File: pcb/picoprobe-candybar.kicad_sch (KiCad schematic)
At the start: 25 parts, among them J1 Conn_IDC_Cable, J2 SWD-UART_PicoprobeCandybar, Q1 BSS806N, SW1 SW-R1-1A-E-1-0, SW2 SLW-156646-5A-N-D, U1 74AUP1T17, U2 74AUP1T17

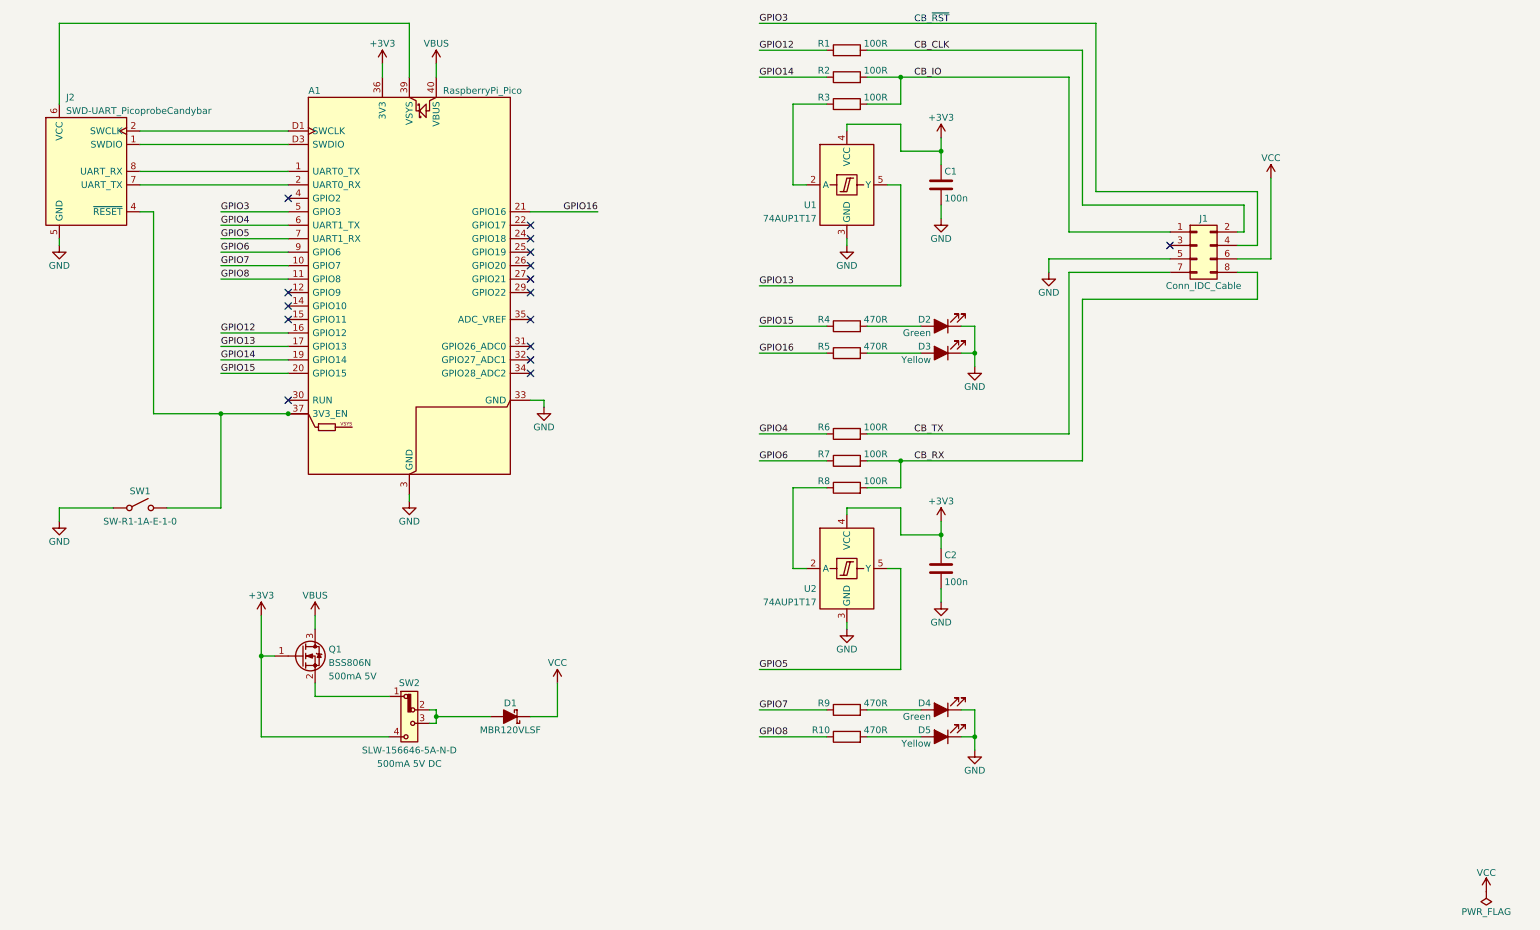
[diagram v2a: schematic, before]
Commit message: Label schematic sections
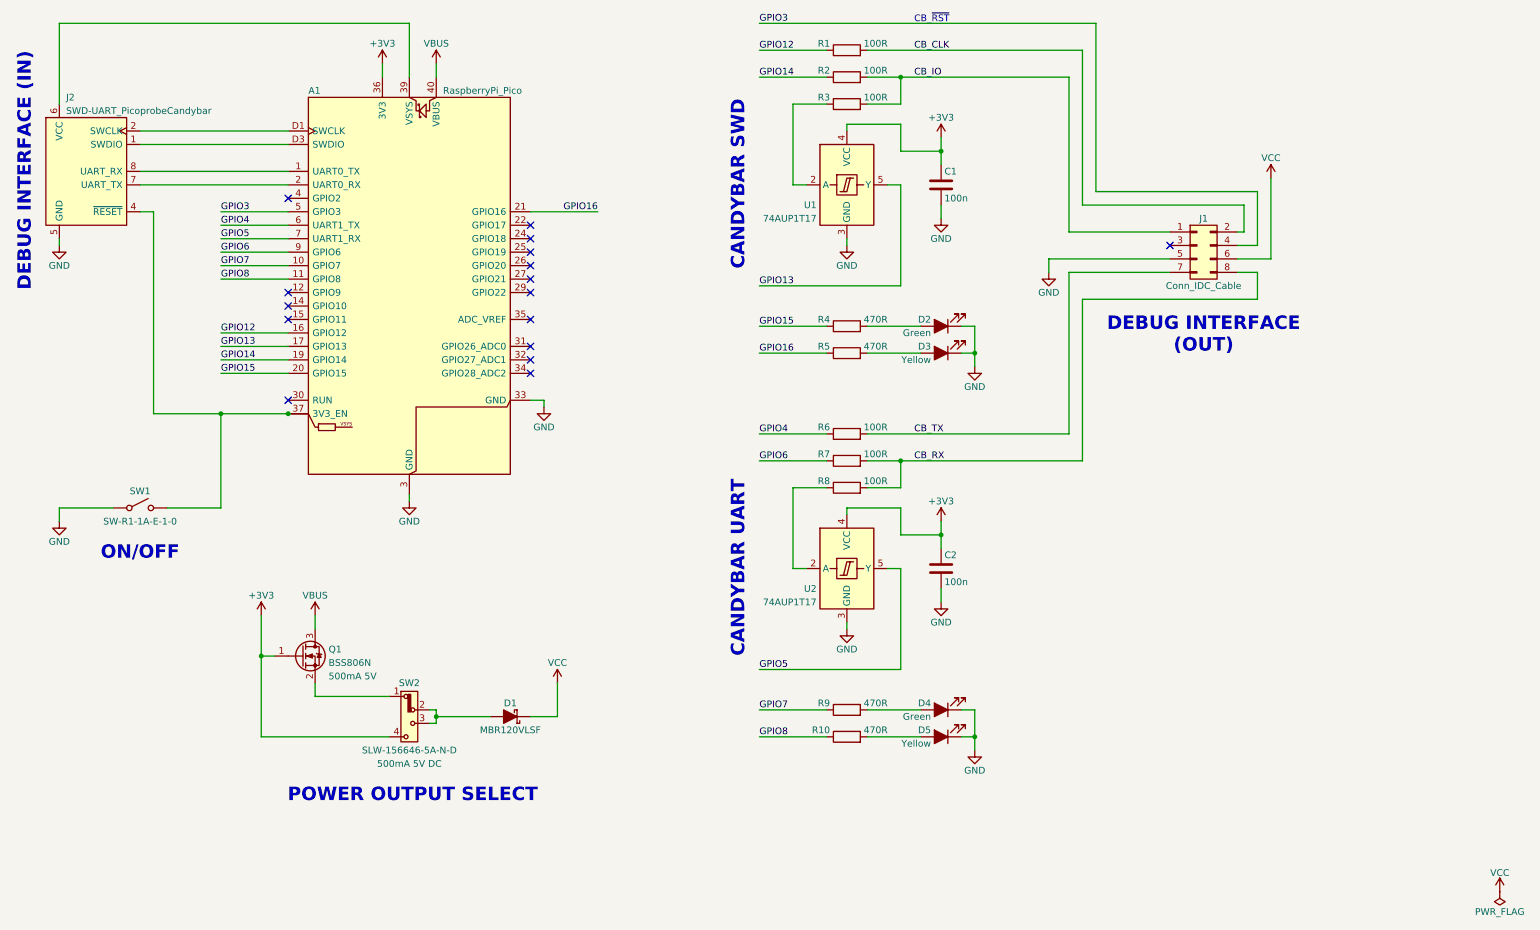
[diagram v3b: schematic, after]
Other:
- note added: "CANDYBAR SWD"
- note added: "CANDYBAR UART"
- note added: "DEBUG INTERFACE (IN)"
- note added: "DEBUG INTERFACE (OUT)"
- note added: "ON/OFF"
- note added: "POWER OUTPUT SELECT"
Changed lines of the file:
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@@
+		)
+	)
+	(text "CANDYBAR UART"
+		(exclude_from_sim no)
+		(at 165.1 129.54 90)
+		(effects
+			(font
+				(size 2.54 2.54)
+				(thickness 0.254)
+				(bold yes)
+			)
+			(justify bottom)
+		)
+	)
+	(text "POWER OUTPUT SELECT"
+		(exclude_from_sim no)
+		(at 102.235 170.815 0)
+		(effects
+			(font
+				(size 2.54 2.54)
+				(thickness 0.254)
+				(bold yes)
+			)
+			(justify top)
 		)
 	)
@@
 			)
 			(justify left bottom)
+		)
+	)
+	(text "DEBUG INTERFACE (IN)"
+		(exclude_from_sim no)
+		(at 30.48 54.61 90)
+		(effects
+			(font
+				(size 2.54 2.54)
+				(thickness 0.254)
+				(bold yes)
+			)
+			(justify bottom)
+		)
+	)
+	(text "ON/OFF"
+		(exclude_from_sim no)
+		(at 50.8 125.095 0)
+		(effects
+			(font
+				(size 2.54 2.54)
+				(thickness 0.254)
+				(bold yes)
+			)
+			(justify top)
+		)
+	)
+	(text "DEBUG INTERFACE\n(OUT)"
+		(exclude_from_sim no)
+		(at 251.46 81.915 0)
+		(effects
+			(font
+				(size 2.54 2.54)
+				(thickness 0.254)
+				(bold yes)
+			)
+			(justify top)
+		)
+	)
+	(text "CANDYBAR SWD"
+		(exclude_from_sim no)
+		(at 165.1 57.15 90)
+		(effects
+			(font
+				(size 2.54 2.54)
+				(thickness 0.254)
+				(bold yes)
+			)
+			(justify bottom)
 		)
 	)
@@
 	(symbol
 		(lib_id "power:PWR_FLAG")
-		(at 304.8 190.5 180)
+		(at 307.34 190.5 180)
 		(unit 1)
 		(exclude_from_sim no)
@@
 		(dnp no)
 		(property "Reference" "#FLG01"
-			(at 304.8 192.405 0)
+			(at 307.34 192.405 0)
 			(effects
 				(font
@@
 		)
 		(property "Value" "PWR_FLAG"
-			(at 304.8 194.31 0)
+			(at 307.34 194.31 0)
 			(effects
 				(font
@@
 		)
 		(property "Footprint" ""
-			(at 304.8 190.5 0)
+			(at 307.34 190.5 0)
 			(effects
 				(font
@@
 		)
 		(property "Datasheet" "~"
-			(at 304.8 190.5 0)
+			(at 307.34 190.5 0)
 			(effects
 				(font
@@
 		)
 		(property "Description" "Special symbol for telling ERC where power comes from"
-			(at 304.8 190.5 0)
+			(at 307.34 190.5 0)
 			(effects
 				(font
@@
 	(symbol
 		(lib_id "power:VCC")
-		(at 304.8 190.5 0)
+		(at 307.34 190.5 0)
 		(unit 1)
 		(exclude_from_sim no)
@@
 		(dnp no)
 		(property "Reference" "#PWR020"
-			(at 304.8 194.31 0)
+			(at 307.34 194.31 0)
 			(effects
 				(font
@@
 		)
 		(property "Value" "VCC"
-			(at 304.8 186.944 0)
+			(at 307.34 186.944 0)
 			(effects
 				(font
@@
 		)
 		(property "Footprint" ""
-			(at 304.8 190.5 0)
+			(at 307.34 190.5 0)
 			(effects
 				(font
@@
 		)
 		(property "Datasheet" ""
-			(at 304.8 190.5 0)
+			(at 307.34 190.5 0)
 			(effects
 				(font
@@
 		)
 		(property "Description" "Power symbol creates a global label with name \"VCC\""
-			(at 304.8 190.5 0)
-			(effects
-				(font
+			(at 307.34 190.5 0)
+			(effects
+				(font

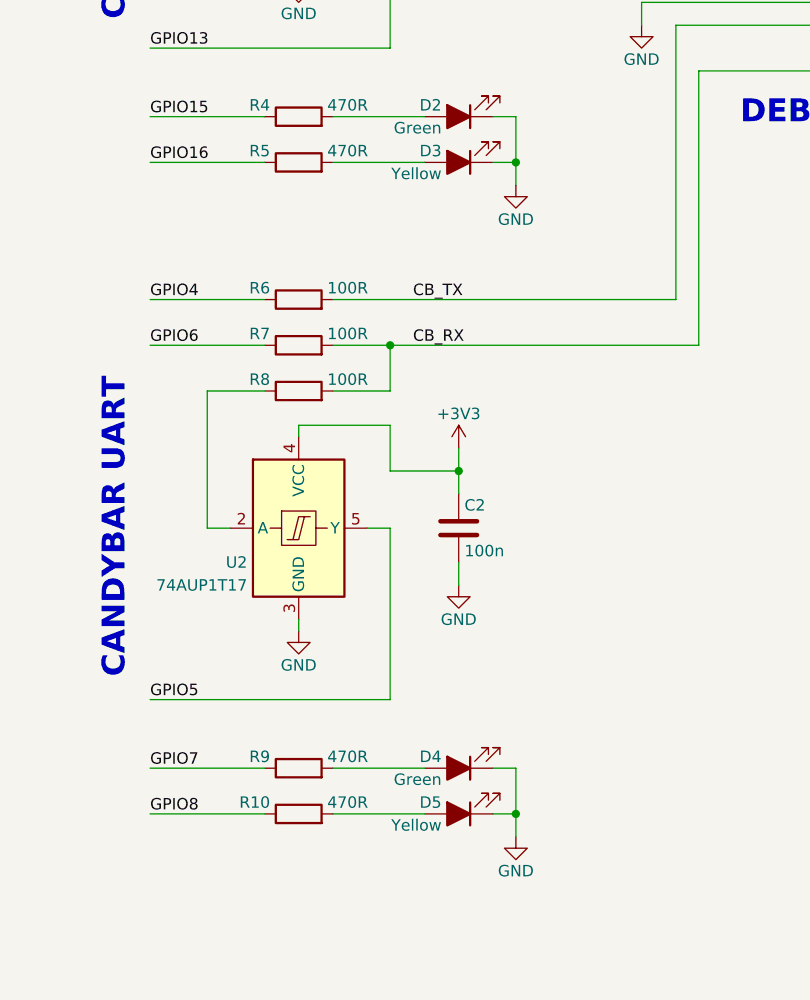
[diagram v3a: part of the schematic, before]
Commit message: Change LED colours
Green: Connected
Orange: Controlling/Transmitting
Yellow: Receiving
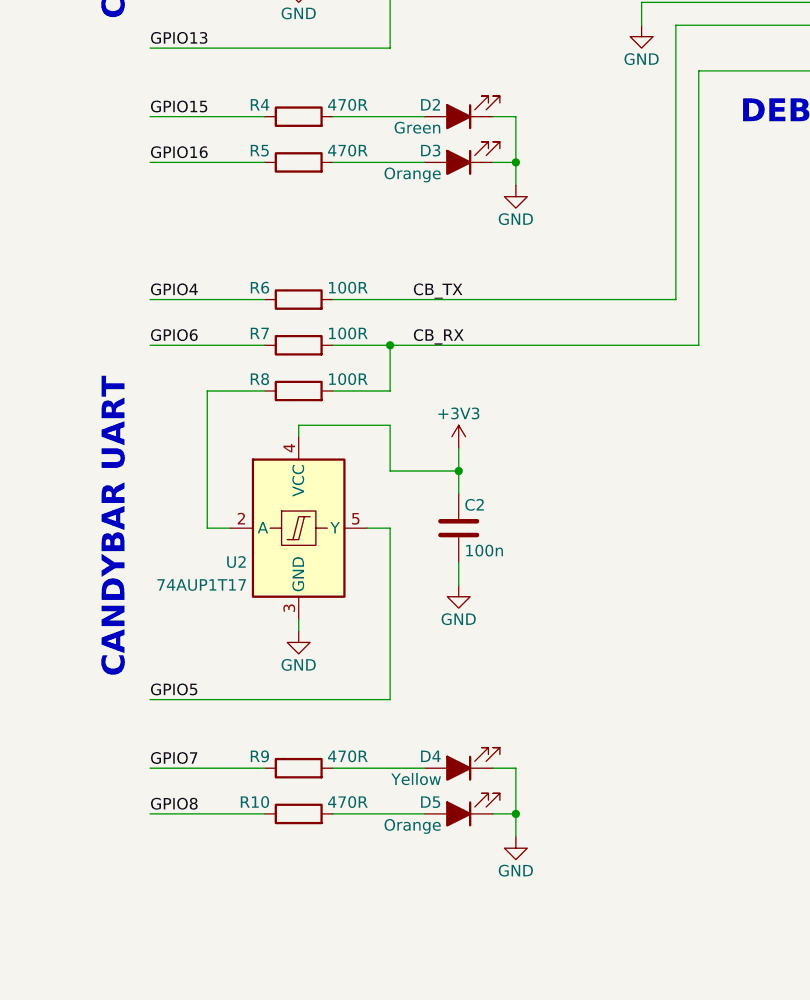
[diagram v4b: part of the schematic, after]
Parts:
- D3, D5: value Yellow -> Orange
- D4: value Green -> Yellow
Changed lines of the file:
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@@
 			)
 		)
-		(property "Value" "Yellow"
+		(property "Value" "Orange"
 			(at 200.025 90.17 0)
 			(effects
@@
 			)
 		)
-		(property "Value" "Yellow"
+		(property "Value" "Orange"
 			(at 200.025 162.56 0)
 			(effects
@@
 			)
 		)
-		(property "Value" "Green"
+		(property "Value" "Yellow"
 			(at 200.025 157.48 0)
 			(effects

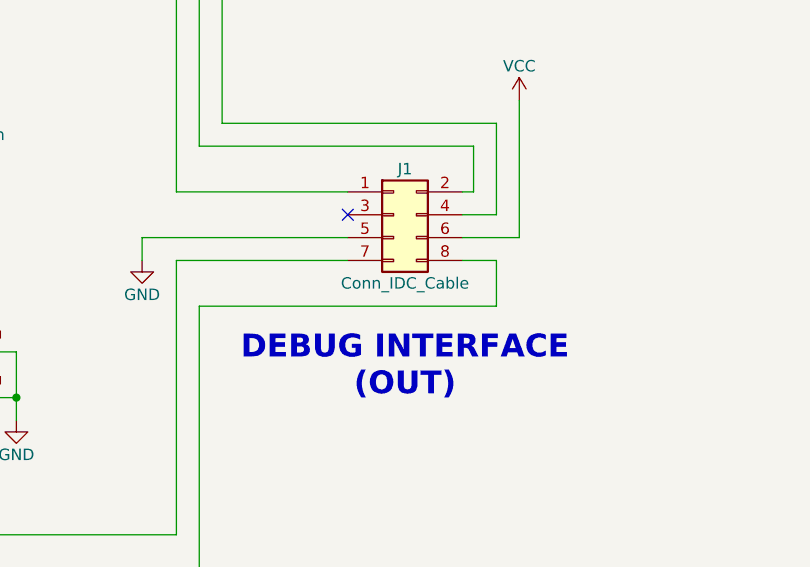
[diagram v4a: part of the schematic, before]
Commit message: Rename IDC header
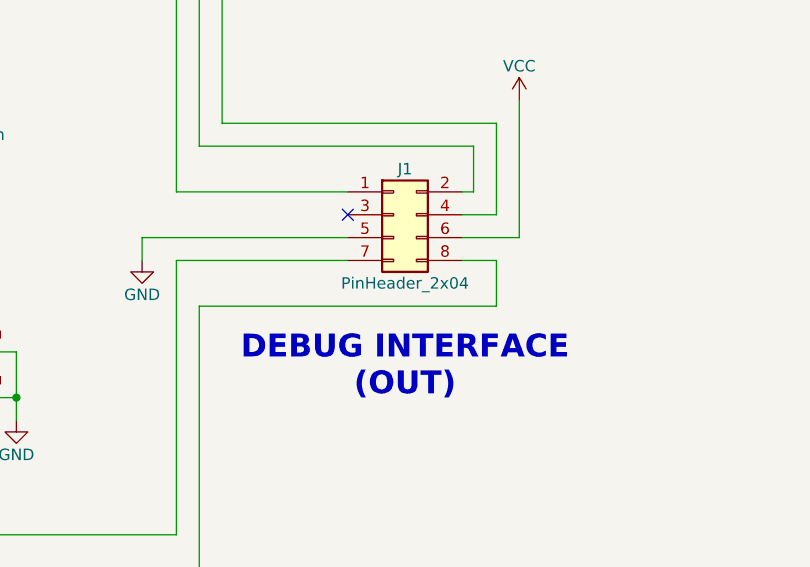
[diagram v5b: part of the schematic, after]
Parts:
- J1: value Conn_IDC_Cable -> PinHeader_2x04
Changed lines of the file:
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@@
 			)
 		)
-		(property "Value" "Conn_IDC_Cable"
+		(property "Value" "PinHeader_2x04"
 			(at 251.46 76.2 0)
 			(effects

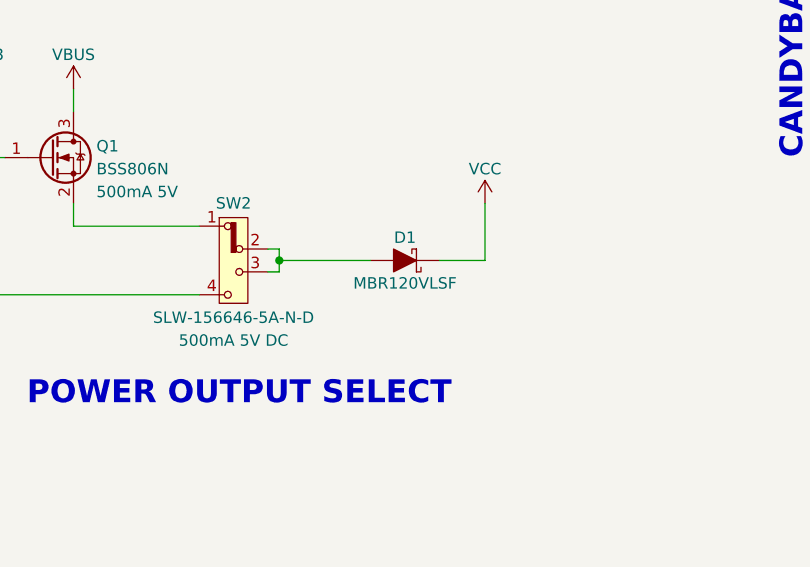
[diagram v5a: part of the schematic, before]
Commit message: Change D1 from MBR120VLSF to PMEG6010ELR
Following suit of the more affordable VBUS protection diode found in the
Raspberry Pi Pico 2

<https://datasheets.raspberrypi.com/pico/pico-2-datasheet.pdf#schematic>
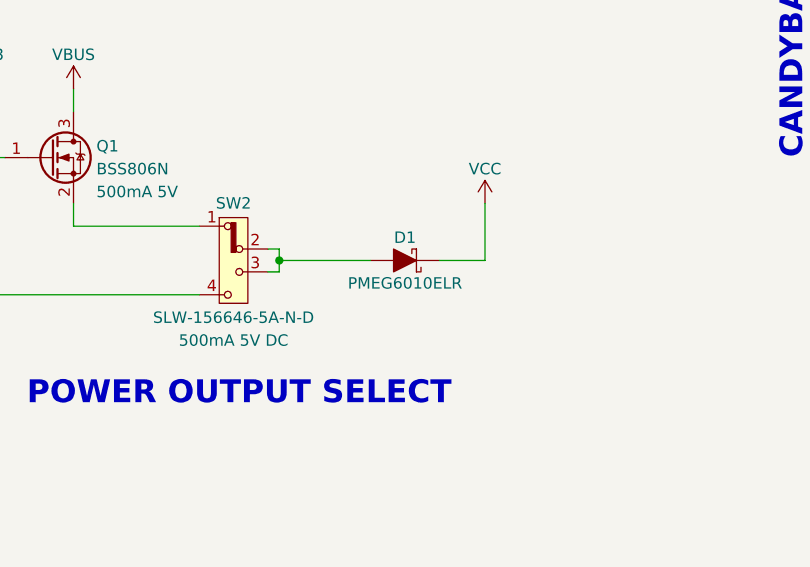
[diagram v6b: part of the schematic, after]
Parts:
- D1: value MBR120VLSF -> PMEG6010ELR; footprint Diode_SMD:D_SOD-123F -> Diode_SMD:Nexperia_CFP3_SOD-123W; symbol ProjectSymbols_PicoprobeCandybar:MBR120VLSF -> ProjectSymbols_PicoprobeCandybar:PMEG6010ELR
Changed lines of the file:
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@@
 	)
 	(symbol
-		(lib_id "ProjectSymbols_PicoprobeCandybar:MBR120VLSF")
+		(lib_id "ProjectSymbols_PicoprobeCandybar:PMEG6010ELR")
 		(at 120.65 157.48 180)
 		(unit 1)
@@
 			)
 		)
-		(property "Value" "MBR120VLSF"
+		(property "Value" "PMEG6010ELR"
 			(at 120.65 160.02 0)
 			(effects
@@
 			)
 		)
-		(property "Footprint" "Diode_SMD:D_SOD-123F"
+		(property "Footprint" "Diode_SMD:Nexperia_CFP3_SOD-123W"
 			(at 120.65 153.035 0)
 			(effects
@@
 			)
 		)
-		(property "Datasheet" "https://www.onsemi.com/pdf/datasheet/mbr120vlsft1-d.pdf"
+		(property "Datasheet" "https://assets.nexperia.com/documents/data-sheet/PMEG6010ELR.pdf"
 			(at 120.65 151.13 0)
 			(effects

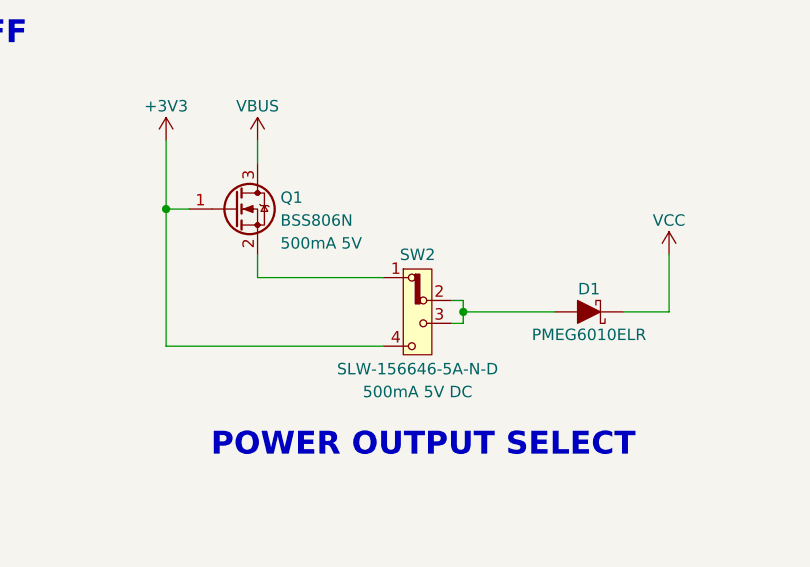
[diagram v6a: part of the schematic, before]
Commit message: Clarify substitutable component constraints
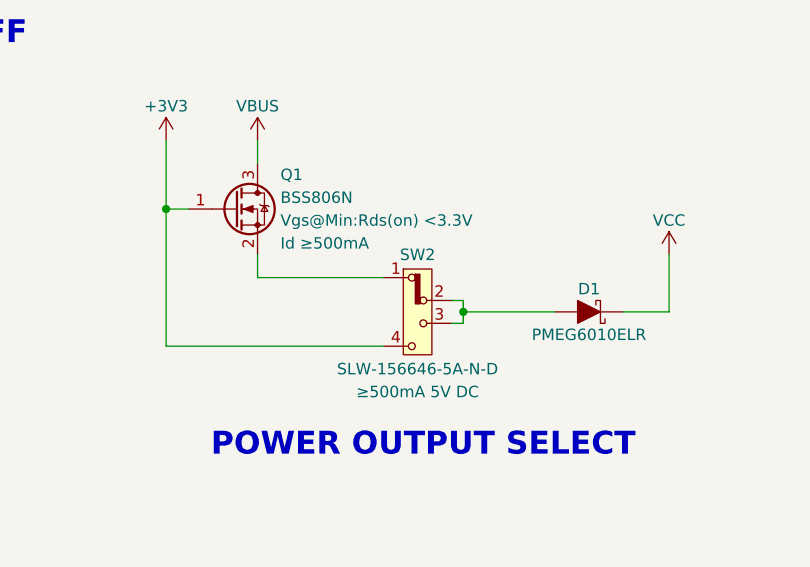
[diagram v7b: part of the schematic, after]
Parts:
- Q1: Specification 500mA 5V -> Vgs@Min:Rds(on) <3.3V; Specification 2 (none) -> Id ≥500mA
- SW2: Specification 500mA 5V DC -> ≥500mA 5V DC
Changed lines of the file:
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@@
 		(dnp no)
 		(property "Reference" "Q1"
+			(at 86.36 142.24 0)
+			(effects
+				(font
+					(size 1.27 1.27)
+				)
+				(justify left)
+			)
+		)
+		(property "Value" "BSS806N"
 			(at 86.36 144.78 0)
-			(effects
-				(font
-					(size 1.27 1.27)
-				)
-				(justify left)
-			)
-		)
-		(property "Value" "BSS806N"
-			(at 86.36 147.32 0)
 			(effects
 				(font
@@
 			)
 		)
-		(property "Specification" "500mA 5V"
+		(property "Specification" "Vgs@Min:Rds(on) <3.3V"
+			(at 86.36 147.32 0)
+			(effects
+				(font
+					(size 1.27 1.27)
+				)
+				(justify left)
+			)
+		)
+		(property "Specification 2" "Id ≥500mA"
 			(at 86.36 149.86 0)
 			(effects
@@
 			)
 		)
-		(property "Specification" "500mA 5V DC"
+		(property "Specification" "≥500mA 5V DC"
 			(at 101.6 166.37 0)
 			(effects
